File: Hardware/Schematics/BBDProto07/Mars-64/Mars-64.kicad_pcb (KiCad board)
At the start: 4 copper layers, 43.2 x 50.8 mm, 76 parts, among them J101 Conn_Coaxial, J102 Conn_Coaxial, U101 ADG731, U102 ADG731

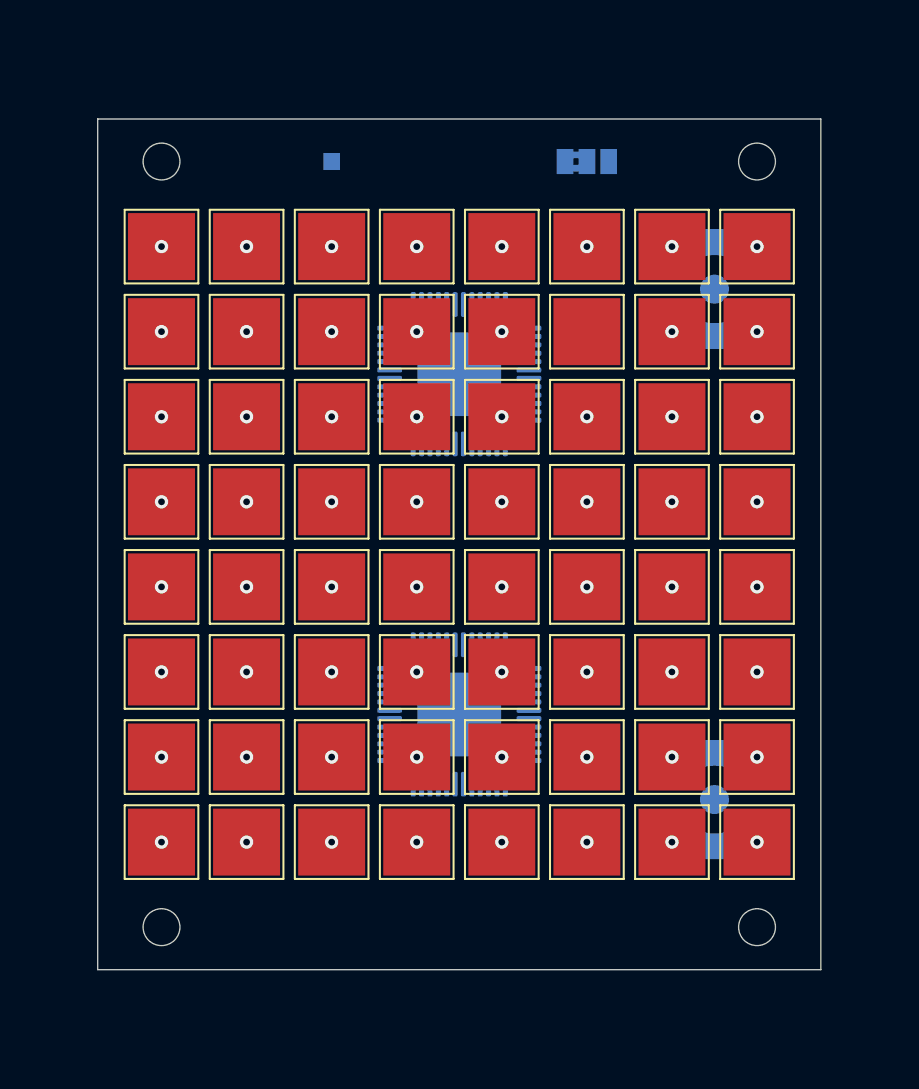
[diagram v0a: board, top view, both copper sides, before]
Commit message: Moved U201 and U202 a little
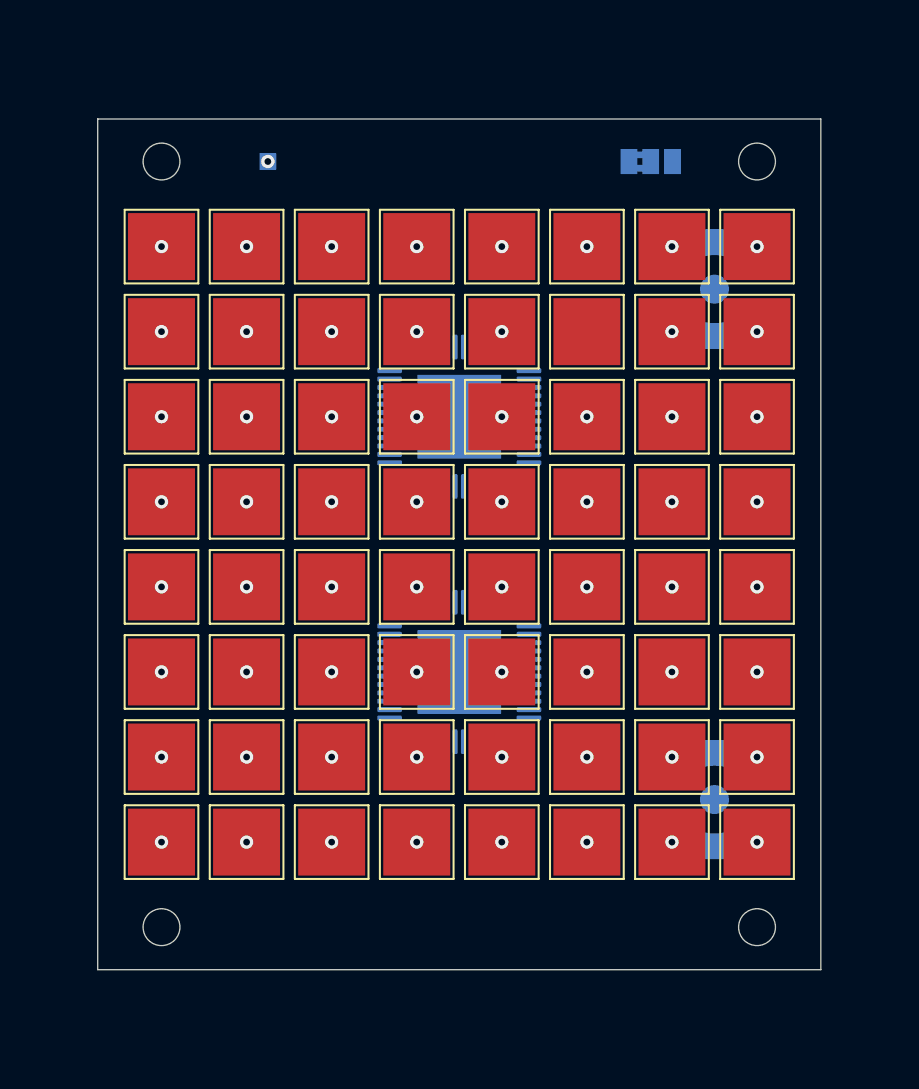
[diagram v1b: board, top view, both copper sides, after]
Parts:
- moved JP4 3.81 mm to (72.4, 33.0)
- moved TPAGND1 3.81 mm to (49.5, 33.0)
- moved U102 2.54 mm to (61.0, 63.5), turned to 180 degrees
- moved U101 2.54 mm to (61.0, 48.3), turned to 180 degrees
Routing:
- net /AGND: vias 0 -> 1

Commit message: Connected the In1.Cu pad to AGND
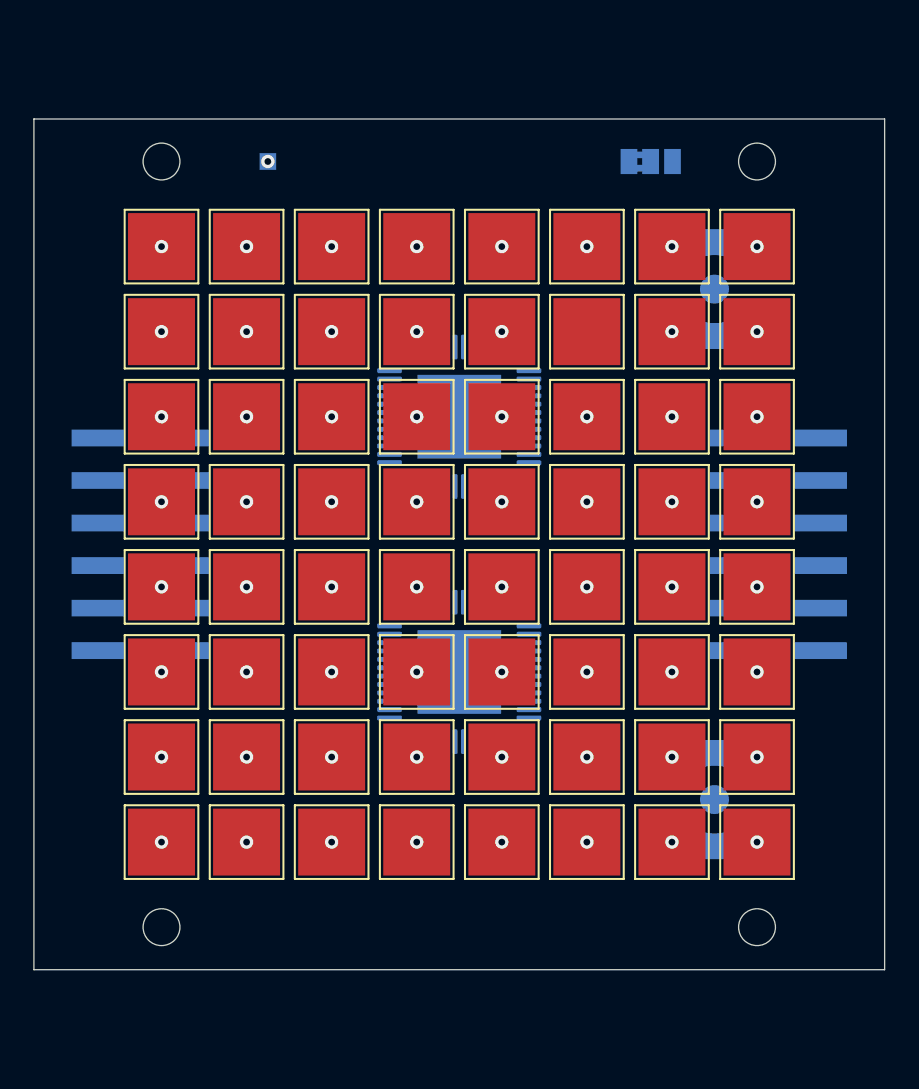
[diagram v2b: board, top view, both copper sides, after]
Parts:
- moved Pmod1 3.81 mm to (80.0, 55.9)
- moved Pmod2 3.81 mm to (41.9, 55.9)
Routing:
- added copper zone on In1.Cu, net /AGND
- removed copper zone on In1.Cu, net (none)
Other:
- board size 43.2 x 50.8 mm -> 50.8 x 50.8 mm
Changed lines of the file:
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@@
   (general
     (thickness 1.6)
-    (drawings 4)
+    (drawings 6)
     (tracks 64)
     (zones 0)
@@
     (solder_mask_min_width 0.25)
     (aux_axis_origin 0 0)
-    (visible_elements 7FFF7FFF)
+    (visible_elements 7FFFFFFF)
     (pcbplotparams
       (layerselection 0x010fc_ffffffff)
@@
   )
   (module Mars-64:PinHeader_2x06_P2.54mm_Vertical_SMD_TopBottom (layer B.Cu)
-    (at 76.2 55.88)
+    (at 80.01 55.88)
     (descr "surface-mounted straight pin header, 2x06, 2.54mm pitch, double rows")
     (tags "Surface mounted pin header SMD 2x06 2.54mm double row")
@@
   )
   (module Mars-64:PinHeader_2x06_P2.54mm_Vertical_SMD_TopBottom_Mirrored (layer B.Cu)
-    (at 45.72 55.88)
+    (at 41.91 55.88)
     (descr "surface-mounted straight pin header, 2x06, 2.54mm pitch, double rows")
     (tags "Surface mounted pin header SMD 2x06 2.54mm double row")
@@
     )
   )
-  (gr_line (start 39.37 30.48) (end 39.37 81.28) (layer Edge.Cuts) (width 0.05))
-  (gr_line (start 82.55 30.48) (end 82.55 81.28) (layer Edge.Cuts) (width 0.05))
-  (gr_line (start 82.55 81.28) (end 39.37 81.28) (layer Edge.Cuts) (width 0.05))
-  (gr_line (start 39.37 30.48) (end 82.55 30.48) (layer Edge.Cuts) (width 0.05))
+  (dimension 50.8 (width 0.15) (layer Dwgs.User)
+    (gr_text "50.800 mm" (at 92.74 55.88 270) (layer Dwgs.User)
+      (effects (font (size 1 1) (thickness 0.15)))
+    )
+    (feature1 (pts (xy 86.36 81.28) (xy 92.026421 81.28)))
+    (feature2 (pts (xy 86.36 30.48) (xy 92.026421 30.48)))
+    (crossbar (pts (xy 91.44 30.48) (xy 91.44 81.28)))
+    (arrow1a (pts (xy 91.44 81.28) (xy 90.853579 80.153496)))
+    (arrow1b (pts (xy 91.44 81.28) (xy 92.026421 80.153496)))
+    (arrow2a (pts (xy 91.44 30.48) (xy 90.853579 31.606504)))
+    (arrow2b (pts (xy 91.44 30.48) (xy 92.026421 31.606504)))
+  )
+  (dimension 50.8 (width 0.15) (layer Dwgs.User)
+    (gr_text "50.800 mm" (at 60.96 24.1) (layer Dwgs.User)
+      (effects (font (size 1 1) (thickness 0.15)))
+    )
+    (feature1 (pts (xy 86.36 30.48) (xy 86.36 24.813579)))
+    (feature2 (pts (xy 35.56 30.48) (xy 35.56 24.813579)))
+    (crossbar (pts (xy 35.56 25.4) (xy 86.36 25.4)))
+    (arrow1a (pts (xy 86.36 25.4) (xy 85.233496 25.986421)))
+    (arrow1b (pts (xy 86.36 25.4) (xy 85.233496 24.813579)))
+    (arrow2a (pts (xy 35.56 25.4) (xy 36.686504 25.986421)))
+    (arrow2b (pts (xy 35.56 25.4) (xy 36.686504 24.813579)))
+  )
+  (gr_line (start 35.56 30.48) (end 35.56 81.28) (layer Edge.Cuts) (width 0.05))
+  (gr_line (start 86.36 30.48) (end 86.36 81.28) (layer Edge.Cuts) (width 0.05))
+  (gr_line (start 86.36 81.28) (end 35.56 81.28) (layer Edge.Cuts) (width 0.05))
+  (gr_line (start 35.56 30.48) (end 86.36 30.48) (layer Edge.Cuts) (width 0.05))
   (via blind (at 49.53 33.02) (size 0.8) (drill 0.4) (layers In1.Cu B.Cu) (net 6))
   (via blind (at 43.18 38.1) (size 0.8) (drill 0.4) (layers F.Cu In2.Cu) (net 9))
@@
   (via blind (at 73.66 73.66) (size 0.8) (drill 0.4) (layers F.Cu In2.Cu) (net 71))
   (via blind (at 78.74 73.66) (size 0.8) (drill 0.4) (layers F.Cu In2.Cu) (net 72))
-  (zone (net 0) (net_name "") (layer In1.Cu) (hatch edge 0.508)
+  (zone (net 6) (net_name /AGND) (layer In1.Cu) (hatch edge 0.508)
     (connect_pads yes (clearance 0.508))
     (min_thickness 0.254)

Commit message: Changed the PCB size to 51x61mm
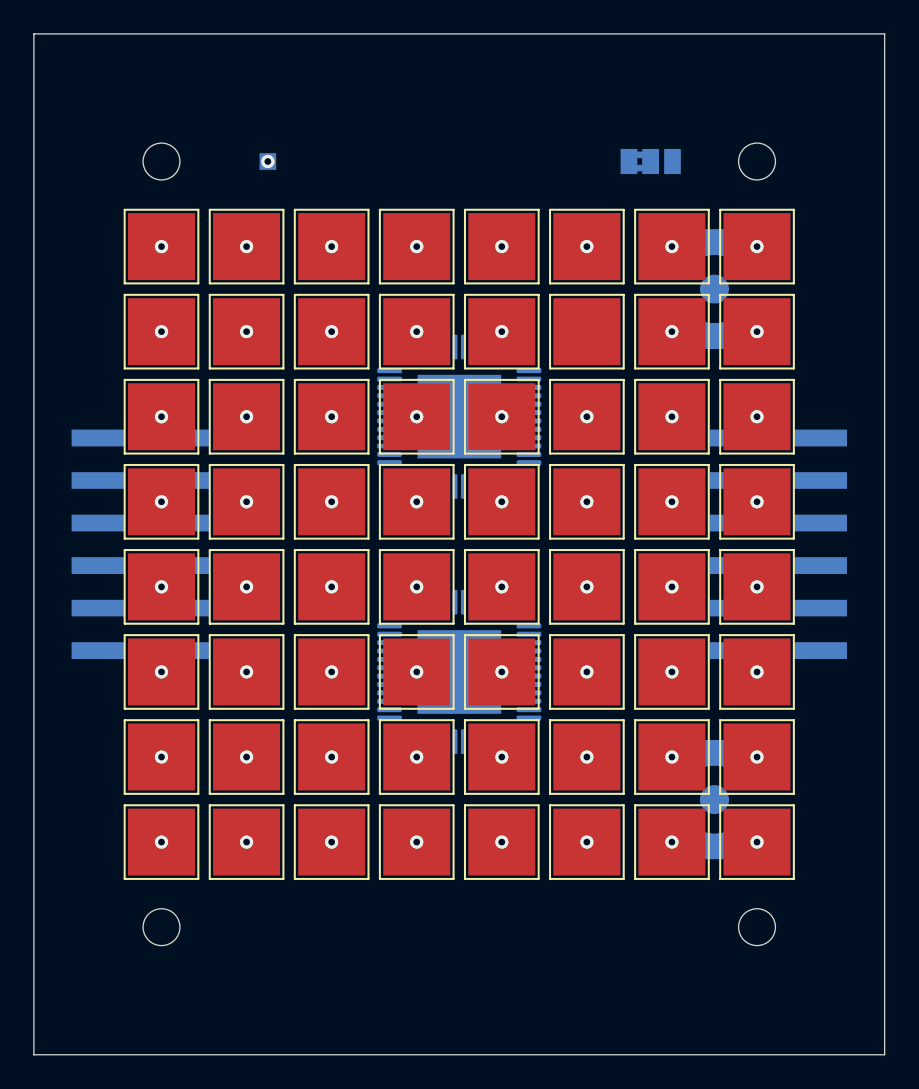
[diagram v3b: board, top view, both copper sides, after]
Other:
- board size 50.8 x 50.8 mm -> 50.8 x 61 mm
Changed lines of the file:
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@@
     )
   )
-  (dimension 50.8 (width 0.15) (layer Dwgs.User)
-    (gr_text "50.800 mm" (at 92.74 55.88 270) (layer Dwgs.User)
+  (dimension 60.96 (width 0.15) (layer Dwgs.User)
+    (gr_text "60.960 mm" (at 92.74 55.88 270) (layer Dwgs.User)
       (effects (font (size 1 1) (thickness 0.15)))
     )
-    (feature1 (pts (xy 86.36 81.28) (xy 92.026421 81.28)))
-    (feature2 (pts (xy 86.36 30.48) (xy 92.026421 30.48)))
-    (crossbar (pts (xy 91.44 30.48) (xy 91.44 81.28)))
-    (arrow1a (pts (xy 91.44 81.28) (xy 90.853579 80.153496)))
-    (arrow1b (pts (xy 91.44 81.28) (xy 92.026421 80.153496)))
-    (arrow2a (pts (xy 91.44 30.48) (xy 90.853579 31.606504)))
-    (arrow2b (pts (xy 91.44 30.48) (xy 92.026421 31.606504)))
+    (feature1 (pts (xy 86.36 86.36) (xy 92.026421 86.36)))
+    (feature2 (pts (xy 86.36 25.4) (xy 92.026421 25.4)))
+    (crossbar (pts (xy 91.44 25.4) (xy 91.44 86.36)))
+    (arrow1a (pts (xy 91.44 86.36) (xy 90.853579 85.233496)))
+    (arrow1b (pts (xy 91.44 86.36) (xy 92.026421 85.233496)))
+    (arrow2a (pts (xy 91.44 25.4) (xy 90.853579 26.526504)))
+    (arrow2b (pts (xy 91.44 25.4) (xy 92.026421 26.526504)))
   )
   (dimension 50.8 (width 0.15) (layer Dwgs.User)
-    (gr_text "50.800 mm" (at 60.96 24.1) (layer Dwgs.User)
+    (gr_text "50.800 mm" (at 60.96 19.02) (layer Dwgs.User)
       (effects (font (size 1 1) (thickness 0.15)))
     )
-    (feature1 (pts (xy 86.36 30.48) (xy 86.36 24.813579)))
-    (feature2 (pts (xy 35.56 30.48) (xy 35.56 24.813579)))
-    (crossbar (pts (xy 35.56 25.4) (xy 86.36 25.4)))
-    (arrow1a (pts (xy 86.36 25.4) (xy 85.233496 25.986421)))
-    (arrow1b (pts (xy 86.36 25.4) (xy 85.233496 24.813579)))
-    (arrow2a (pts (xy 35.56 25.4) (xy 36.686504 25.986421)))
-    (arrow2b (pts (xy 35.56 25.4) (xy 36.686504 24.813579)))
+    (feature1 (pts (xy 86.36 25.4) (xy 86.36 19.733579)))
+    (feature2 (pts (xy 35.56 25.4) (xy 35.56 19.733579)))
+    (crossbar (pts (xy 35.56 20.32) (xy 86.36 20.32)))
+    (arrow1a (pts (xy 86.36 20.32) (xy 85.233496 20.906421)))
+    (arrow1b (pts (xy 86.36 20.32) (xy 85.233496 19.733579)))
+    (arrow2a (pts (xy 35.56 20.32) (xy 36.686504 20.906421)))
+    (arrow2b (pts (xy 35.56 20.32) (xy 36.686504 19.733579)))
   )
-  (gr_line (start 35.56 30.48) (end 35.56 81.28) (layer Edge.Cuts) (width 0.05))
-  (gr_line (start 86.36 30.48) (end 86.36 81.28) (layer Edge.Cuts) (width 0.05))
-  (gr_line (start 86.36 81.28) (end 35.56 81.28) (layer Edge.Cuts) (width 0.05))
-  (gr_line (start 35.56 30.48) (end 86.36 30.48) (layer Edge.Cuts) (width 0.05))
+  (gr_line (start 35.56 25.4) (end 35.56 86.36) (layer Edge.Cuts) (width 0.05))
+  (gr_line (start 86.36 25.4) (end 86.36 86.36) (layer Edge.Cuts) (width 0.05))
+  (gr_line (start 86.36 86.36) (end 35.56 86.36) (layer Edge.Cuts) (width 0.05))
+  (gr_line (start 35.56 25.4) (end 86.36 25.4) (layer Edge.Cuts) (width 0.05))
   (via blind (at 49.53 33.02) (size 0.8) (drill 0.4) (layers In1.Cu B.Cu) (net 6))
   (via blind (at 43.18 38.1) (size 0.8) (drill 0.4) (layers F.Cu In2.Cu) (net 9))

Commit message: Moved the mounting points and added a few AGND vias to the board
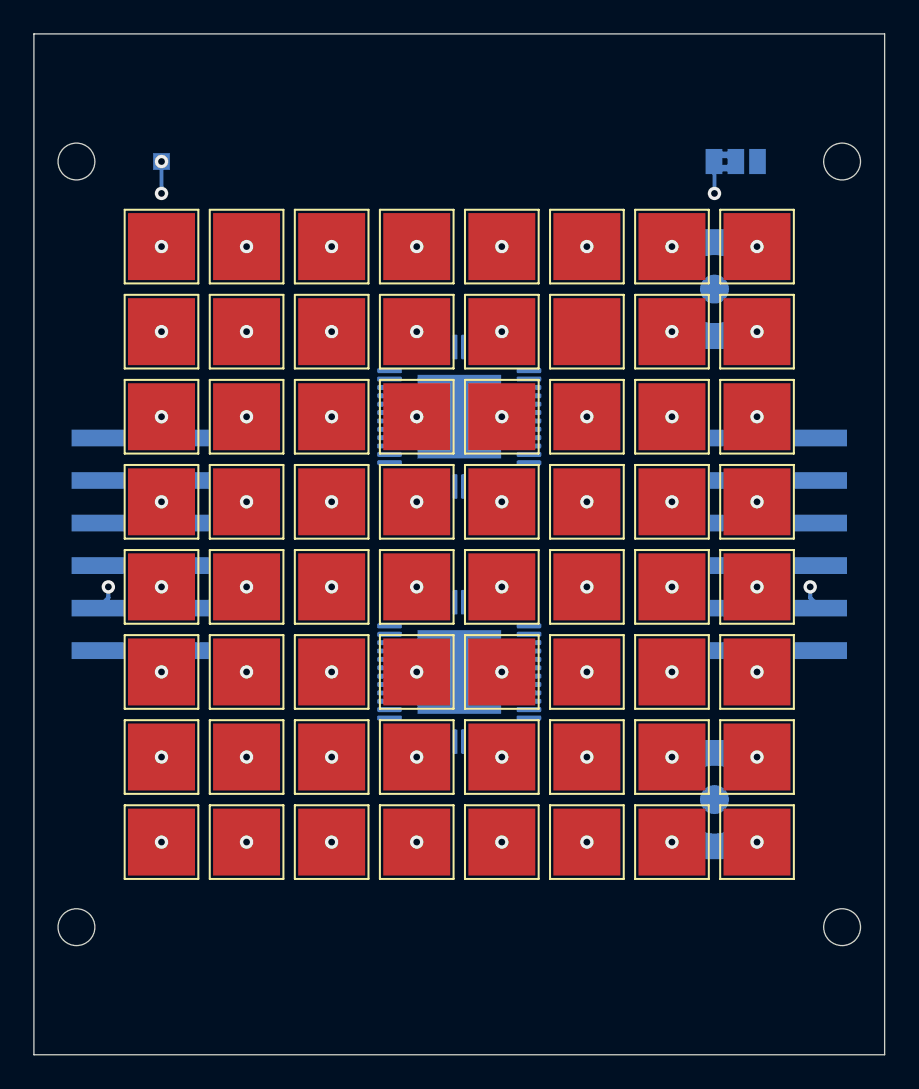
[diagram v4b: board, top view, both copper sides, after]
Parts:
- moved TPAGND1 6.35 mm to (43.2, 33.0)
- moved H1 5.08 mm to (38.1, 33.0)
- moved H2 5.08 mm to (83.8, 33.0)
- moved H3 5.08 mm to (38.1, 78.7)
- moved H4 5.08 mm to (83.8, 78.7)
- moved JP4 5.08 mm to (77.5, 33.0)
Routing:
- net /AGND: track 0.00 -> 6.88 mm, vias 1 -> 5
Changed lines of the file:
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@@
     (thickness 1.6)
     (drawings 6)
-    (tracks 64)
+    (tracks 75)
     (zones 0)
     (modules 76)
@@
   )
   (module MountingHole:MountingHole_2.2mm_M2 (layer F.Cu)
-    (at 43.18 33.02)
+    (at 38.1 33.02)
     (descr "Mounting Hole 2.2mm, no annular, M2")
     (tags "mounting hole 2.2mm no annular m2")
@@
   )
   (module MountingHole:MountingHole_2.2mm_M2 (layer F.Cu)
-    (at 78.74 33.02)
+    (at 83.82 33.02)
     (descr "Mounting Hole 2.2mm, no annular, M2")
     (tags "mounting hole 2.2mm no annular m2")
@@
   )
   (module MountingHole:MountingHole_2.2mm_M2 (layer F.Cu)
-    (at 43.18 78.74)
+    (at 38.1 78.74)
     (descr "Mounting Hole 2.2mm, no annular, M2")
     (tags "mounting hole 2.2mm no annular m2")
@@
   )
   (module MountingHole:MountingHole_2.2mm_M2 (layer F.Cu)
-    (at 78.74 78.74)
+    (at 83.82 78.74)
     (descr "Mounting Hole 2.2mm, no annular, M2")
     (tags "mounting hole 2.2mm no annular m2")
@@
   )
   (module TestPoint:TestPoint_Pad_1.0x1.0mm (layer B.Cu)
-    (at 49.53 33.02)
+    (at 43.18 33.02)
     (descr "SMD rectangular pad as test Point, square 1.0mm side length")
     (tags "test point SMD pad rectangle square")
@@
   )
   (module Jumper:SolderJumper-3_P1.3mm_Bridged2Bar12_Pad1.0x1.5mm_NumberLabels (layer B.Cu)
-    (at 72.39 33.02)
+    (at 77.47 33.02)
     (descr "SMD Solder Jumper, 1x1.5mm Pads, 0.3mm gap, pads 1-2 Bridged2Bar with 2 copper strip, labeled with numbers")
     (tags "solder jumper open")
@@
   (gr_line (start 86.36 86.36) (end 35.56 86.36) (layer Edge.Cuts) (width 0.05))
   (gr_line (start 35.56 25.4) (end 86.36 25.4) (layer Edge.Cuts) (width 0.05))
-  (via blind (at 49.53 33.02) (size 0.8) (drill 0.4) (layers In1.Cu B.Cu) (net 6))
+  (via blind (at 40.005 58.42) (size 0.8) (drill 0.4) (layers In1.Cu B.Cu) (net 6))
+  (via blind (at 81.915 58.42) (size 0.8) (drill 0.4) (layers In1.Cu B.Cu) (net 6))
+  (via blind (at 76.2 34.925) (size 0.8) (drill 0.4) (layers In1.Cu B.Cu) (net 6))
+  (via blind (at 43.18 34.925) (size 0.8) (drill 0.4) (layers In1.Cu B.Cu) (net 6))
+  (via blind (at 43.18 33.02) (size 0.8) (drill 0.4) (layers In1.Cu B.Cu) (net 6))
+  (segment (start 81.915 59.07) (end 82.535 59.69) (width 0.25) (layer B.Cu) (net 6))
+  (segment (start 81.915 58.42) (end 81.915 59.07) (width 0.25) (layer B.Cu) (net 6))
+  (segment (start 40.005 59.07) (end 39.385 59.69) (width 0.25) (layer B.Cu) (net 6))
+  (segment (start 40.005 58.42) (end 40.005 59.07) (width 0.25) (layer B.Cu) (net 6))
+  (segment (start 43.18 34.925) (end 43.18 33.02) (width 0.25) (layer B.Cu) (net 6))
+  (segment (start 76.2 33.05) (end 76.17 33.02) (width 0.25) (layer B.Cu) (net 6))
+  (segment (start 76.2 34.925) (end 76.2 33.05) (width 0.25) (layer B.Cu) (net 6))
   (via blind (at 43.18 38.1) (size 0.8) (drill 0.4) (layers F.Cu In2.Cu) (net 9))
   (via blind (at 48.26 38.1) (size 0.8) (drill 0.4) (layers F.Cu In2.Cu) (net 10))
@@
     (connect_pads yes (clearance 0.508))
     (min_thickness 0.254)
-    (fill (arc_segments 32) (thermal_gap 0.508) (thermal_bridge_width 0.508))
+    (fill yes (arc_segments 32) (thermal_gap 0.508) (thermal_bridge_width 0.508))
     (polygon
       (pts
-        (xy 81.28 76.2) (xy 40.64 76.2) (xy 40.64 35.56) (xy 81.28 35.56)
+        (xy 82.55 77.47) (xy 39.37 77.47) (xy 39.37 34.29) (xy 82.55 34.29)
       )
     )

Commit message: Finished up the missing routes, ready to manufacturing
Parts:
- moved U101 5.68 mm to (58.4, 43.2)
- moved U102 5.68 mm to (58.4, 68.6), turned to 0 degrees
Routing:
- net GND: track 0.00 -> 110.2 mm, vias 0 -> 2
- net /VCC3V3: track 0.00 -> 85.2 mm, vias 0 -> 2
- net Net-(TP217-Pad1): track 0.00 -> 83.9 mm, vias 1 -> 2
- net Net-(TP208-Pad1): track 0.00 -> 82.4 mm, vias 1 -> 2
- net /SPI_CLK: track 0.00 -> 78.6 mm, vias 0 -> 3
- net Net-(TP123-Pad1): track 0.00 -> 70.9 mm, vias 1 -> 2
- net Net-(TP101-Pad1): track 0.00 -> 69.0 mm, vias 1 -> 2
- net /~SPI_CE: track 0.00 -> 64.3 mm, vias 0 -> 2
- net /DA: track 0.00 -> 63.2 mm, vias 0 -> 2
- net Net-(TP119-Pad1): track 0.00 -> 62.1 mm, vias 1 -> 2
- net /DB: track 0.00 -> 61.7 mm, vias 0 -> 2
- net Net-(TP122-Pad1): track 0.00 -> 61.3 mm, vias 1 -> 2
- net Net-(J101-Pad2): track 0.00 -> 61.0 mm, vias 0 -> 2
- net Net-(TP111-Pad1): track 0.00 -> 60.2 mm, vias 1 -> 2
- net Net-(TP120-Pad1): track 0.00 -> 59.2 mm, vias 1 -> 2
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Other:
- board size 50.8 x 61 mm -> 50.8 x 50.8 mm
